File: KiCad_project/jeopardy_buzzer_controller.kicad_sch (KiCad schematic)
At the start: 19 parts, among them J10 Conn_01x02_Male, J11 ENABLE_SW, J12 ENABLE_LED, J13 PWR_LED, J14 Conn_01x02_Male, J9 Conn_01x02_Male, SW1 RESET, SW2 Enable_switch, U1 Arduino Pro Micro

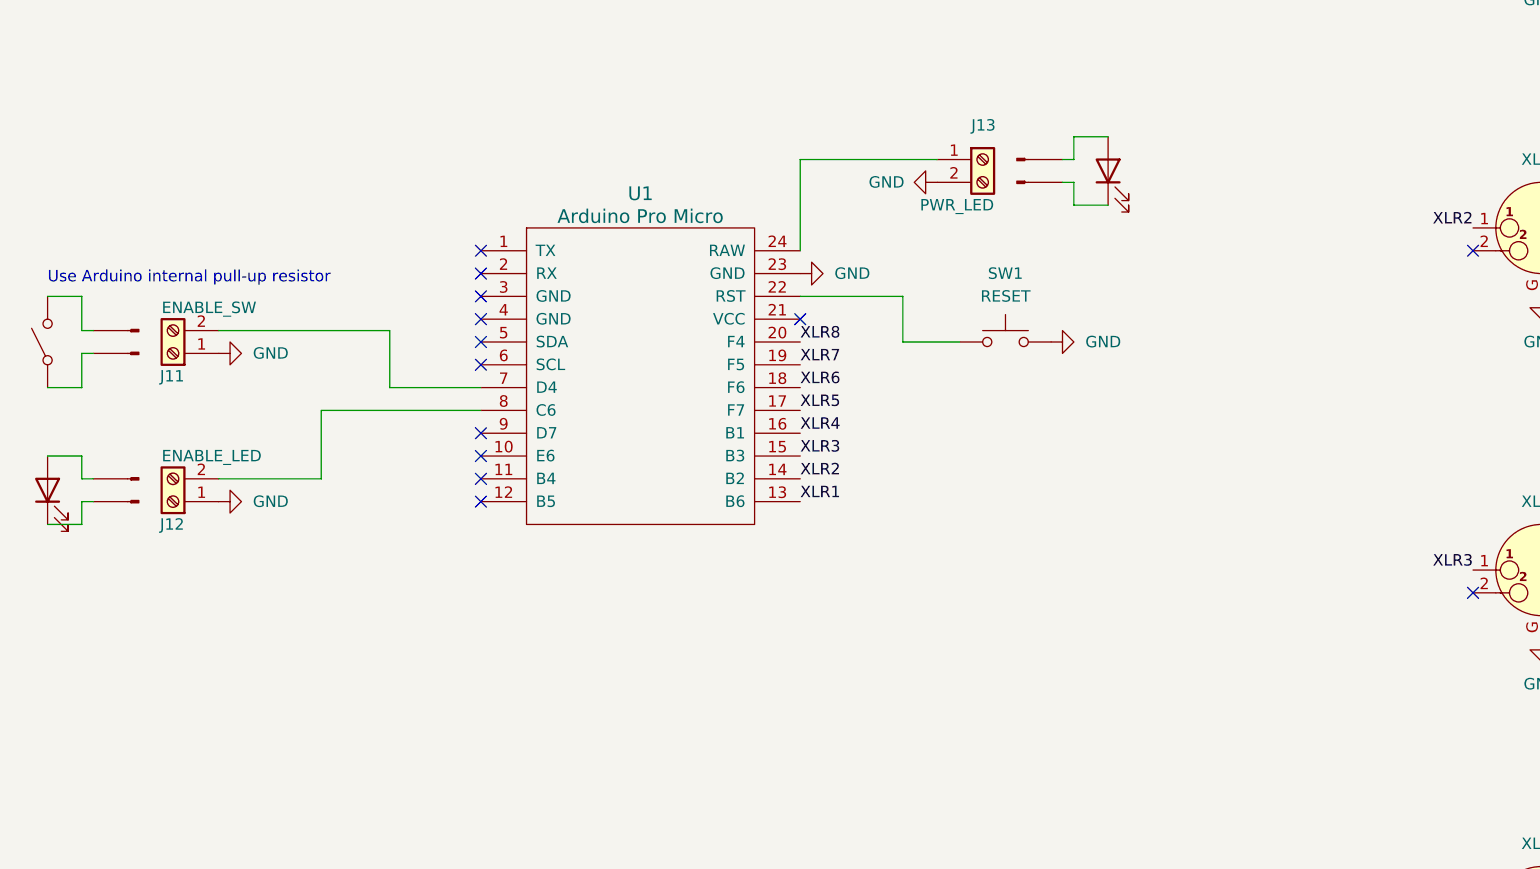
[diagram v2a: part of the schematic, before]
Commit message: Fix pin mapping between KiCad and Arduino
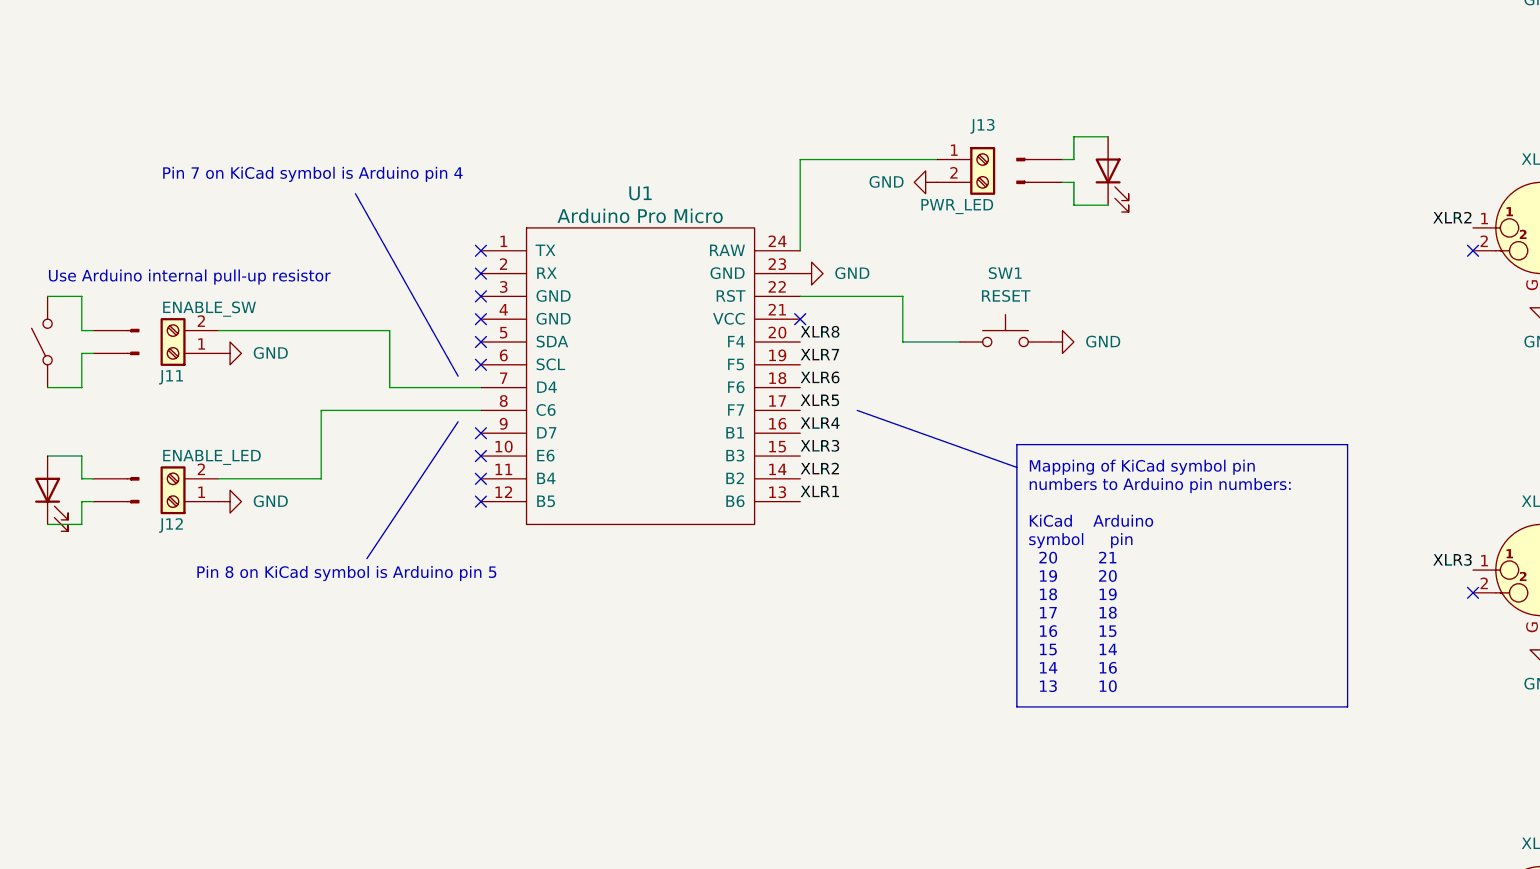
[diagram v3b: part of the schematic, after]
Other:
- note added: "Mapping of KiCad symbol pin numbers to Arduino pin numbers: KiCad Arduino symbol pin 20 21 19 20 18 19 17 18 16 15 15 14 14 16 13 10"
- note added: "Pin 7 on KiCad symbol is Arduino pin 4"
- note added: "Pin 8 on KiCad symbol is Arduino pin 5"
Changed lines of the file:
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@@
+    (stroke (width 0) (type default) (color 0 0 0 0))
+  )
+  (polyline (pts (xy 144.78 95.25) (xy 181.61 95.25))
     (stroke (width 0) (type default) (color 0 0 0 0))
   )
@@
     (stroke (width 0) (type default) (color 0 0 0 0))
   )
+  (polyline (pts (xy 181.61 95.25) (xy 181.61 124.46))
+    (stroke (width 0) (type default) (color 0 0 0 0))
+  )
   (wire (pts (xy 120.65 78.74) (xy 132.08 78.74))
     (stroke (width 0) (type default) (color 0 0 0 0))
@@
     (stroke (width 0) (type default) (color 0 0 0 0))
   )
+  (polyline (pts (xy 127 91.44) (xy 144.78 97.79))
+    (stroke (width 0) (type default) (color 0 0 0 0))
+  )
   (wire (pts (xy 74.93 88.9) (xy 74.93 82.55))
     (stroke (width 0) (type default) (color 0 0 0 0))
@@
     (stroke (width 0) (type default) (color 0 0 0 0))
   )
+  (polyline (pts (xy 144.78 95.25) (xy 144.78 124.46))
+    (stroke (width 0) (type default) (color 0 0 0 0))
+  )
   (wire (pts (xy 40.64 88.9) (xy 36.83 88.9))
+    (stroke (width 0) (type default) (color 0 0 0 0))
+  )
+  (polyline (pts (xy 181.61 124.46) (xy 144.78 124.46))
     (stroke (width 0) (type default) (color 0 0 0 0))
   )
@@
     (stroke (width 0) (type default) (color 0 0 0 0))
   )
+  (polyline (pts (xy 82.55 87.63) (xy 71.12 67.31))
+    (stroke (width 0) (type default) (color 0 0 0 0))
+  )
   (wire (pts (xy 40.64 82.55) (xy 40.64 78.74))
     (stroke (width 0) (type default) (color 0 0 0 0))
@@
     (stroke (width 0) (type default) (color 0 0 0 0))
   )
+  (polyline (pts (xy 82.55 92.71) (xy 72.39 107.95))
+    (stroke (width 0) (type default) (color 0 0 0 0))
+  )
   (text "Use Arduino internal pull-up resistor" (at 36.83 77.47 0)
     (effects (font (size 1.27 1.27)) (justify left bottom))
@@
     (effects (font (size 1.27 1.27)) (justify left bottom))
   )
+  (text "Pin 8 on KiCad symbol is Arduino pin 5" (at 53.34 110.49 0)
+    (effects (font (size 1.27 1.27)) (justify left bottom))
+  )
+  (text "Pin 7 on KiCad symbol is Arduino pin 4" (at 49.53 66.04 0)
+    (effects (font (size 1.27 1.27)) (justify left bottom))
+  )
+  (text "Mapping of KiCad symbol pin\nnumbers to Arduino pin numbers:\n\nKiCad    Arduino\nsymbol     pin\n  20        21\n  19        20\n  18        19\n  17        18\n  16        15\n  15        14\n  14        16\n  13        10"
+    (at 146.05 123.19 0)
+    (effects (font (size 1.27 1.27)) (justify left bottom))
+  )
